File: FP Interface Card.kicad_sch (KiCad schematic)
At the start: 7 parts, among them J1 T1M-05-GF-DV, J2 T2M-105-01-X-D-TH-DS, P1 Card Edge for HSEC8-160-01-S-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

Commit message: design updates
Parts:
- removed J1: T1M-05-GF-DV, symbol Connector_Generic:Conn_01x10
- removed J2: T2M-105-01-X-D-TH-DS, payload-interface-board:SAMTEC_T2M-105-01-X-D-TH-DS, symbol Connector_Generic:Conn_01x10
- removed J?: T1M-03-GF-DV, symbol Connector_Generic:Conn_02x03_Odd_Even
- added J4: T1M-6-F-SV-L, payload-interface-board:SAMTEC_T1M-06-F-SV-L, symbol Connector_Generic:Conn_01x06
- added Q17, Q18, Q20, Q22: MMBT4401-7-F, Package_TO_SOT_SMD:SOT-23, symbol Device:Q_NPN_BEC
- added Q19, Q21, Q23: IRF7404TRPBF, Package_SO:SO-8_3.9x4.9mm_P1.27mm, symbol SLI-Backplane-Blank-Card-KiCad:IRF7404TRPBF
- added R100, R103, R106, R89: 10k, Resistor_SMD:R_0603_1608Metric, symbol Device:R_US
- added R101, R104, R107: 3.3k, Resistor_SMD:R_0603_1608Metric, symbol Device:R_US
- added R102, R105, R44, R94, R99: 100k, Resistor_SMD:R_0603_1608Metric, symbol Device:R_US
- added R90, R91, R92, R93, R95, R96, R97, R98: 0, Resistor_SMD:R_0603_1608Metric, symbol Device:R_US
- added U24: RockBlock_9603, payload-interface-board:RockBlock_9603, symbol FP-Interface-Card:RockBlock_9603
- J1: renamed from J?; value T2M-105-01-X-D-TH-DS -> T1M-10-F-SV-L; footprint payload-interface-board:SAMTEC_T2M-105-01-X-D-TH-DS -> payload-interface-board:SAMTEC_T1M-10-F-SV-L
- J2, J5: renamed from J?; value T1M-05-GF-DV -> T1M-10-F-SV-L; footprint (none) -> payload-interface-board:SAMTEC_T1M-10-F-SV-L
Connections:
- net RB_rx is gone; now on net RB_OnOff: J1.7 (Pin_7)
- net +5V: now also Q21.1 (S), Q21.2 (S), Q21.3 (S), Q23.1 (S), Q23.2 (S), Q23.3 (S), R104.1, R107.1
- net 5V_RF: now also Q19.1 (S), Q19.2 (S), Q19.3 (S), R101.1, R94.1; no longer J1.1 (Pin_1), J1.2 (Pin_2)
- net GND: now also J2.10 (Pin_10), J2.8 (Pin_8), J2.9 (Pin_9), J5.10 (Pin_10), J5.8 (Pin_8), J5.9 (Pin_9), Q17.2 (E), Q18.2 (E), Q20.2 (E), Q22.2 (E), R102.2, R105.2, R44.2, R99.2, U24.1 (MH); no longer J1.9 (Pin_9)
- net H1-11: now also R105.1, R106.1
- net H2-24: now also R102.1, R103.1
- net Level Shifter 5/io_hi: now also R97.1, R98.1
- net Level Shifter 6/io_hi: now also R95.1, R96.1
- net RB_CTS: now also J1.2 (Pin_2)
- net RB_OnOff: now also Q17.3 (C), R94.2; no longer J1.8 (Pin_8)
- net RB_RTS: now also J1.3 (Pin_3)
- net SERVO_PWR_CTRL: now also J5.7 (Pin_7)
- net X+: now also J4.2 (Pin_2)
- net X-: now also J4.1 (Pin_1)
- net Y+: now also J4.4 (Pin_4)
- net Y-: now also J4.3 (Pin_3)
- net Z+: now also J4.6 (Pin_6)
- net Z-: now also J4.5 (Pin_5)
- net ST_5V: now reaches J2.1 (Pin_1)
- net ST_5V: now also J2.2 (Pin_2), J2.3 (Pin_3), Q21.5 (D), Q21.6 (D), Q21.7 (D), Q21.8 (D)
- net ST_RST: now reaches J2.4 (Pin_4)
- net ST_TXD: now reaches J2.5 (Pin_5)
- net ST_TXD: now also R90.2, R92.2
- net ST_RXD: now reaches J2.6 (Pin_6)
- net ST_RXD: now also R91.2, R93.2
- net RB_NetAv: now reaches J1.4 (Pin_4)
- net RB_RI: now reaches J1.5 (Pin_5)
- net PAYLOAD_5V: now reaches J5.1 (Pin_1)
- net PAYLOAD_5V: now also J5.2 (Pin_2), J5.3 (Pin_3), Q23.5 (D), Q23.6 (D), Q23.7 (D), Q23.8 (D)
- net P_RESET: now reaches J5.4 (Pin_4)
- net P_TXD: now reaches J5.5 (Pin_5)
- net P_RXD: now reaches J5.6 (Pin_6)
- net RB_tx renamed RB_TxD
- net RB_TxD: now also R96.2, R98.2
- new net: Q20.3 (C), Q21.4 (G), R104.2
- new net: Q22.3 (C), Q23.4 (G), R107.2
- new net: Q18.3 (C), Q19.4 (G), R101.2
- new net: Q17.1 (B), R89.2
- new net H1-07: R100.1, R99.1
- new net H1-08: R44.1, R89.1
- new net Level Shifter 7/io_hi: R90.1, R91.1
- new net Level Shifter 8/io_hi: R92.1, R93.1
- new net PAYLOAD_PWR_SW: Q20.1 (B), Q22.1 (B), R103.2, R106.2
- new net RB_5V_IN: J1.8 (Pin_8), Q19.5 (D), Q19.6 (D), Q19.7 (D), Q19.8 (D)
- new net RB_Li-iON: J1.9 (Pin_9)
- new net RB_PWR_SW_B: Q18.1 (B), R100.2
- new net RB_RxD: J1.1 (Pin_1), R95.2, R97.2
- no-connect marks 4 -> 5
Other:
- added sheet Pico (pico.kicad_sch)
- note added: "DNP!!"
- note added: "PICO"
- note added: "RB has a low power sleep, but this is to disconnect in case of failure."
- note added: "ROCKBLOCK LEVEL SHIFTERS & POWER SW"
- note added: "STAR TRACKER LEVEL SHIFTERS & POWER SW"
- note added: "TO ROCKBLOCK 9603"
- note added: "UART_3_Rx"
- note added: "UART_3_Tx"
- note added: "UART_4_Rx"
- note added: "UART_4_Tx"
- note added: "mainboard PB16"
- note added: "mainboard PC05"
- note added: "mainboard PC06"
- note added: "mainboard PC07"
- note added: "mainboard PC10"
- note added: "mainboard PC11"
- note removed: "ROCKBLOCK LEVEL SHIFTERS"
- note removed: "TO ROCKBLOCK 9602"
- note removed: "mainboard PC01"
- note removed: "make rockblock sch symbol and FP"
- note removed: "pull'd high by servo power regulator?"
- moved on the sheet: J1, J2, J5

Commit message: friday changes
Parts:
- removed J2: T1M-10-F-SV-L, payload-interface-board:SAMTEC_T1M-10-F-SV-L, symbol Connector_Generic:Conn_02x05_Odd_Even
- removed Q20: MMBT4401-7-F, Package_TO_SOT_SMD:SOT-23, symbol Device:Q_NPN_BEC
- removed Q21: IRF7404TRPBF, Package_SO:SO-8_3.9x4.9mm_P1.27mm, symbol SLI-Backplane-Blank-Card-KiCad:IRF7404TRPBF
- removed R102: 100k, Resistor_SMD:R_0603_1608Metric, symbol Device:R_US
- removed R103: 10k, Resistor_SMD:R_0603_1608Metric, symbol Device:R_US
- removed R104: 3.3k, Resistor_SMD:R_0603_1608Metric, symbol Device:R_US
- removed R90, R91, R92, R93: 0, Resistor_SMD:R_0603_1608Metric, symbol Device:R_US
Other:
- removed sheet Level Shifter 7
- removed sheet Level Shifter 8
- removed sheet Level Shifter 9
- note removed: "STAR TRACKER LEVEL SHIFTERS & POWER SW"
- note removed: "TO STAR TRACKER"
- note removed: "UART_4_Rx"
- note removed: "UART_4_Tx"
- note removed: "mainboard PB16"
- note removed: "mainboard PC11"
- moved on the sheet: Q17, R44, R89, R94

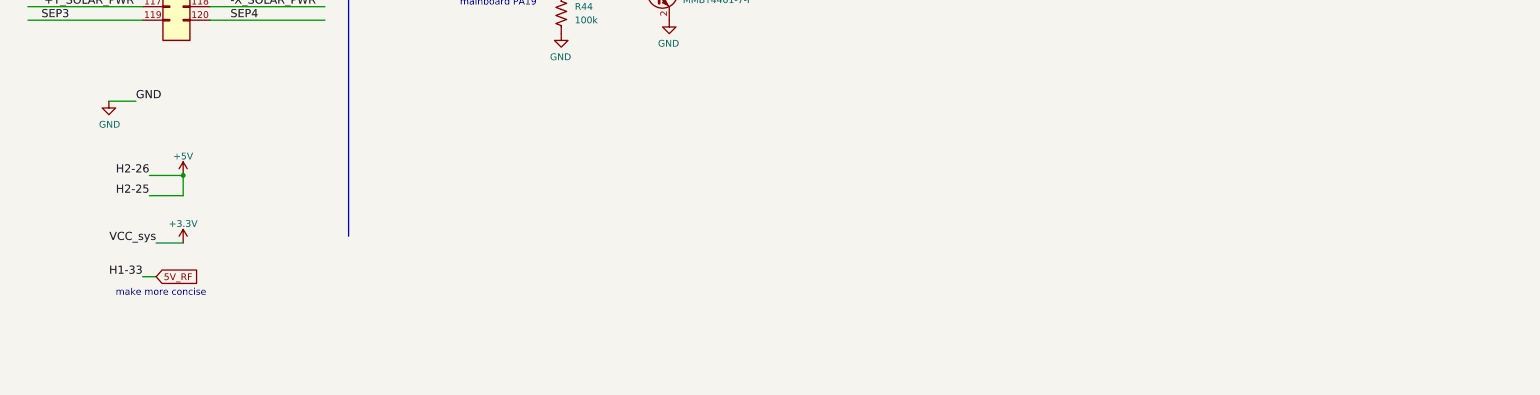
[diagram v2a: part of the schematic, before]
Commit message: added current sensors and other design changes
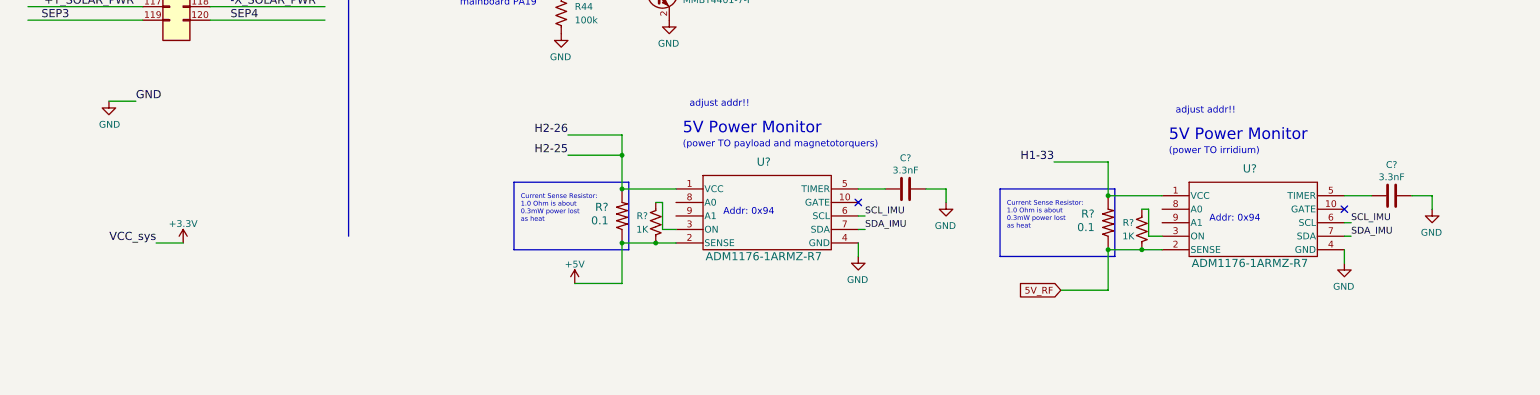
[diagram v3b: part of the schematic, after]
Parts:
- added C? (x2): 3.3nF, Capacitor_SMD:C_0603_1608Metric, symbol mainboard-rescue:C-Device-mainboard-rescue
- added R? (x2): 0.1, Resistor_SMD:R_2512_6332Metric, symbol mainboard:R-US_R2512
- added R? (x2): 1K, Resistor_SMD:R_0603_1608Metric, symbol mainboard-rescue:R_US-Device-mainboard-rescue
- added U? (x2): ADM1176-1ARMZ-R7, mainboard:ADM1176-1ARMZ-R7, symbol mainboard:ADM1176-1ARMZ-R7
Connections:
- net +5V: now also R?.1, R?.1, U?.2 (SENSE); no longer P1.59 (Pin_59), P1.60 (Pin_60)
- net 5V_RF: now also R?.1, R?.1, U?.2 (SENSE); no longer P1.73 (Pin_73)
- net GND: now also C?.1, C?.1, U?.4 (GND), U?.4 (GND)
- net SCL_IMU: now also U?.6 (SCL), U?.6 (SCL)
- net SDA_IMU: now also U?.7 (SDA), U?.7 (SDA)
- new net: C?.2, U?.5 (TIMER) (x2)
- new net: R?.2, U?.3 (ON) (x2)
- new net H1-33: P1.73 (Pin_73), R?.2, U?.1 (VCC)
- new net H2-25: P1.59 (Pin_59), P1.60 (Pin_60), R?.2, U?.1 (VCC)
- no-connect marks 5 -> 7
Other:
- note added: "(power TO irridium)"
- note added: "(power TO payload and magnetotorquers)"
- note added: "5V Power Monitor"
- note added: "Addr: 0x94"
- note added: "Current Sense Resistor: 1.0 Ohm is about 0.3mW power lost as heat"
- note added: "adjust addr!!"
- note removed: "make more concise"

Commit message: finished routing
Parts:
- removed C? (x2): 3.3nF, Capacitor_SMD:C_0603_1608Metric, symbol mainboard-rescue:C-Device-mainboard-rescue
- removed R? (x2): 0.1, Resistor_SMD:R_2512_6332Metric, symbol mainboard:R-US_R2512
- removed R? (x2): 1K, Resistor_SMD:R_0603_1608Metric, symbol mainboard-rescue:R_US-Device-mainboard-rescue
- removed U? (x2): ADM1176-1ARMZ-R7, mainboard:ADM1176-1ARMZ-R7, symbol mainboard:ADM1176-1ARMZ-R7
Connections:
- net H1-07 is gone; now on net H1-7: R100.1, R99.1
- net H1-08 is gone; now on net H1-8: R44.1, R89.1
- net H1-33 is gone; now on net 5V_RF: P1.73 (Pin_73)
- net H2-25 is gone; now on net +5V: P1.59 (Pin_59), P1.60 (Pin_60)
- no-connect marks 7 -> 5
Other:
- note removed: "(power TO irridium)"
- note removed: "(power TO payload and magnetotorquers)"
- note removed: "5V Power Monitor"
- note removed: "Addr: 0x94"
- note removed: "Current Sense Resistor: 1.0 Ohm is about 0.3mW power lost as heat"
- note removed: "adjust addr!!"
